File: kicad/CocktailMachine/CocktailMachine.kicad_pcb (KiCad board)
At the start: 2 copper layers, 66 parts, among them J1 Conn_01x08_Male, J2 0022232041, J3 3220-10-0100-00, J4 Barrel_Jack_Switch, J5 105-1102-001, J6 105-1103-001, J7 0022232041, U1 ESP32-WROOM-32, U2 TXB0104PWR, U3 MCP6477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

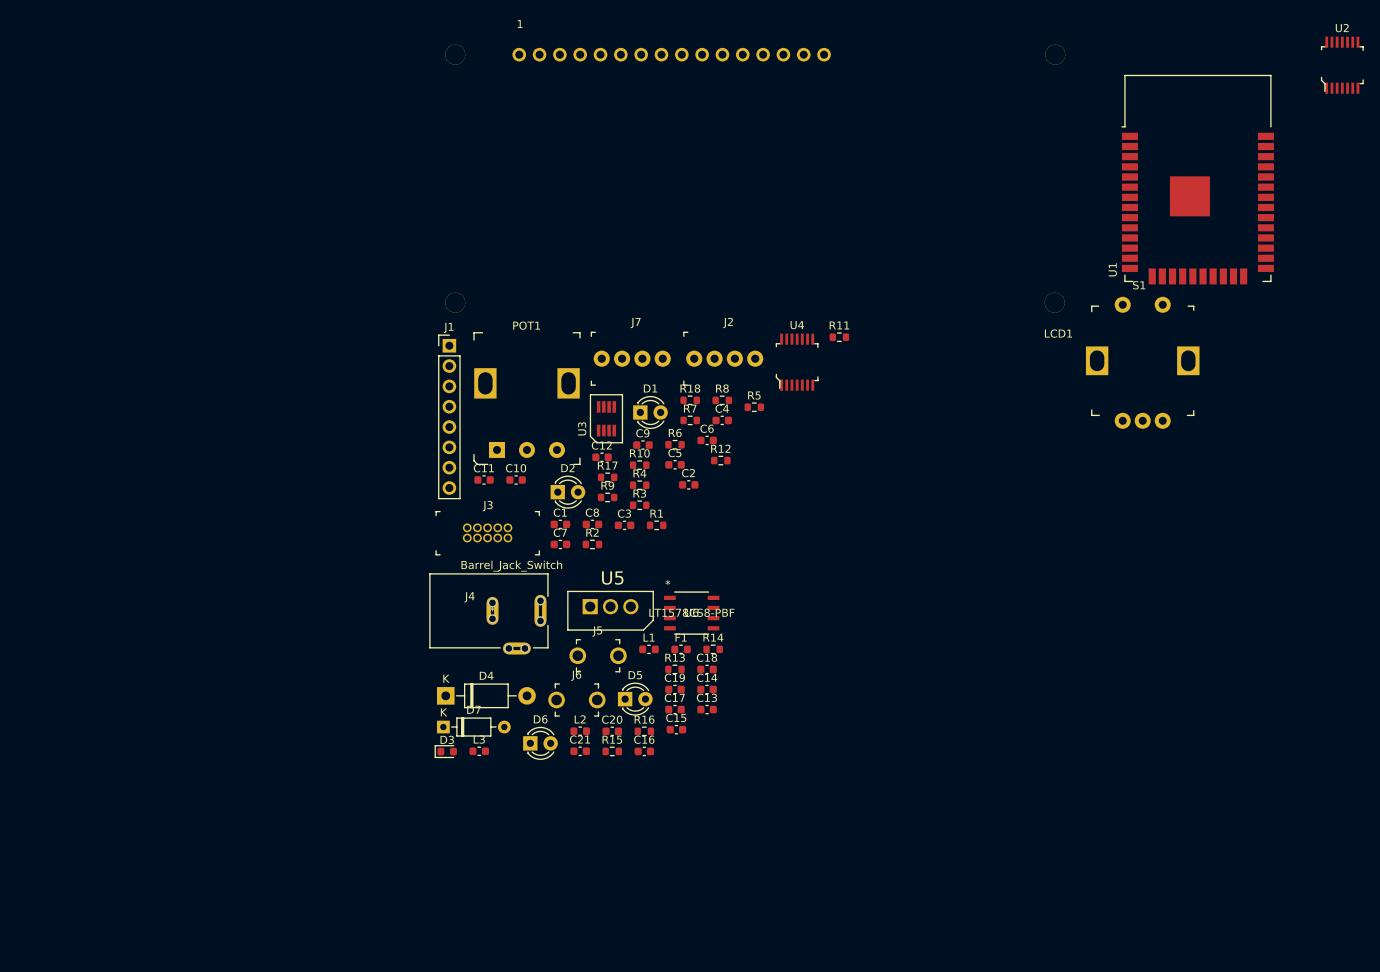
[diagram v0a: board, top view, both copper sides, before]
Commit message: - Update symbol and footprint library - Update obsolete components - Initial layout positioning done. Todo: routing
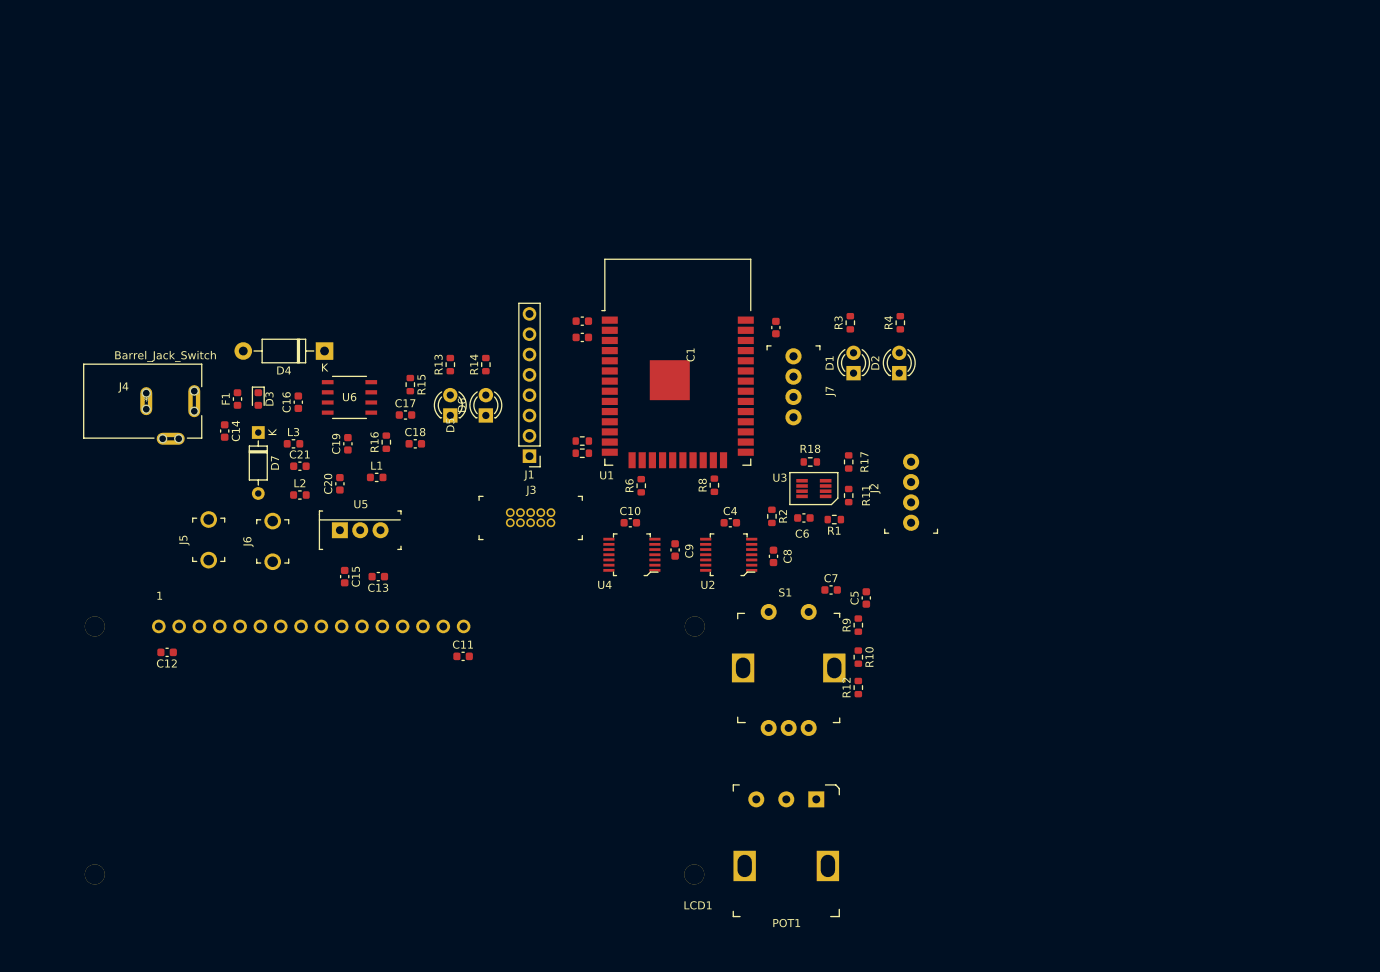
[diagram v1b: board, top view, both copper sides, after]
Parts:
- U5: value MCP1826S-3302e/AB -> LD1117V33; footprint MCP1826S-3302E_AB:TO254P482X1024X3124-3P -> digikey-footprints:TO-220-3
- moved U2 98.1 mm to (135.8, 89.2), turned to 90 degrees
- moved LCD1 84.5 mm to (95.6, 114.2)
- moved U1 69.0 mm to (129.4, 68.1)
- moved C14 68.4 mm to (72.8, 73.7), turned to -90 degrees
- moved F1 63.7 mm to (74.4, 69.7), turned to 90 degrees
- moved C16 61.5 mm to (82.0, 70.1), turned to 90 degrees
- moved C12 59.6 mm to (65.6, 101.4), turned to 180 degrees
- moved POT1 59.2 mm to (146.8, 119.8), turned to 180 degrees
- moved S1 58.6 mm to (137.6, 103.3)
- moved R15 52.3 mm to (96.0, 67.9), turned to -90 degrees
- moved C19 51.1 mm to (88.2, 75.3), turned to 90 degrees
- moved J5 50.8 mm to (70.8, 87.3), turned to 90 degrees
- moved J4 50.6 mm to (63.0, 70.0)
- moved U6 50.6 mm to (88.4, 69.5)
- moved D3 50.0 mm to (77.0, 69.7), turned to -90 degrees
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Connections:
- J3 pad 10: Net-(J3-Pad10) -> unconnected-(J3-Pad10)
- J3 pad 7: Net-(J3-Pad7) -> unconnected-(J3-Pad7)
- LCD1 pad 10: Net-(LCD1-Pad10) -> unconnected-(LCD1-Pad10)
- LCD1 pad 7: Net-(LCD1-Pad7) -> unconnected-(LCD1-Pad7)
- LCD1 pad 8: Net-(LCD1-Pad8) -> unconnected-(LCD1-Pad8)
- LCD1 pad 9: Net-(LCD1-Pad9) -> unconnected-(LCD1-Pad9)
- POT1 pad 2: Net-(POT1-Pad2) -> unconnected-(POT1-Pad2)
- POT1 pad 4: Net-(POT1-Pad4) -> unconnected-(POT1-Pad4)
- U1 pad 29: Net-(U1-Pad29) -> unconnected-(U1-Pad29)
- U1 pad 32: Net-(U1-Pad32) -> unconnected-(U1-Pad32)
- U1 pad 36: Net-(U1-Pad36) -> unconnected-(U1-Pad36)
- U2 pad 10: Net-(U2-Pad10) -> unconnected-(U2-Pad10)
- U2 pad 5: Net-(U2-Pad5) -> unconnected-(U2-Pad5)
- U2 pad 6: Net-(U2-Pad6) -> unconnected-(U2-Pad6)
- U2 pad 9: Net-(U2-Pad9) -> unconnected-(U2-Pad9)
- U4 pad 6: Net-(U4-Pad6) -> unconnected-(U4-Pad6)
- U4 pad 9: Net-(U4-Pad9) -> unconnected-(U4-Pad9)
- U5 pad 1: +5V -> GND
- U5 pad 2: GND -> +3V3
- U5 pad 3: +3V3 -> +5V
- U6 pad 7: Net-(U6-Pad7) -> unconnected-(U6-Pad7)
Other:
- net class Default removed

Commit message: - Fix DRC violations - Shrink space between modules to reduce board size
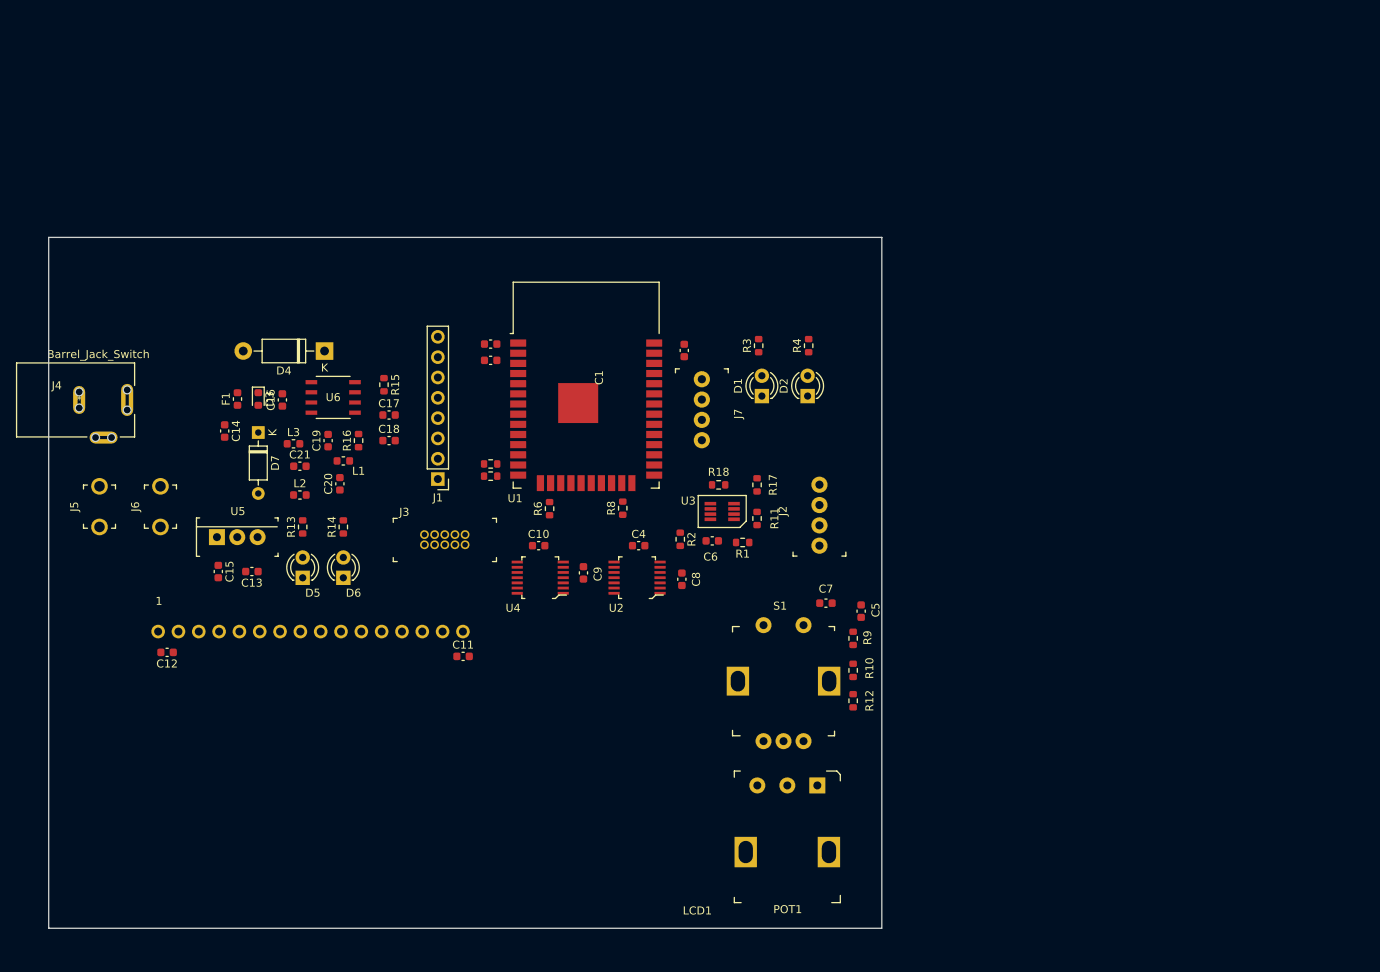
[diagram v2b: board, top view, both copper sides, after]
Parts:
- moved D5 27.4 mm to (82.5, 92.1)
- moved R13 27.4 mm to (82.5, 85.7)
- moved D6 27.0 mm to (87.6, 92.1)
- moved R14 27.0 mm to (87.6, 85.7)
- moved C13 15.8 mm to (76.2, 91.3)
- moved C15 15.8 mm to (72.0, 91.3)
- moved U5 15.4 mm to (71.8, 87.0)
- moved J6 14.7 mm to (64.8, 83.2)
- moved J5 14.3 mm to (57.1, 83.2)
- moved J7 11.8 mm to (132.4, 67.3)
- moved R1 11.8 mm to (137.5, 87.7)
- moved R11 11.8 mm to (139.3, 84.7)
- moved R17 11.8 mm to (139.3, 80.5)
- moved R18 11.8 mm to (134.5, 80.5)
- moved C8 11.8 mm to (129.9, 92.3)
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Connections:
- POT1 pad 2: unconnected-(POT1-Pad2) -> /V0_DISPLAY_CONTRAST
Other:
- board outline added: 104.1 x 86.4 mm

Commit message: - Finish layout - Fixed all DRC violations minus silkscreen issues - Updated via sizes to meet PCBWay requirements
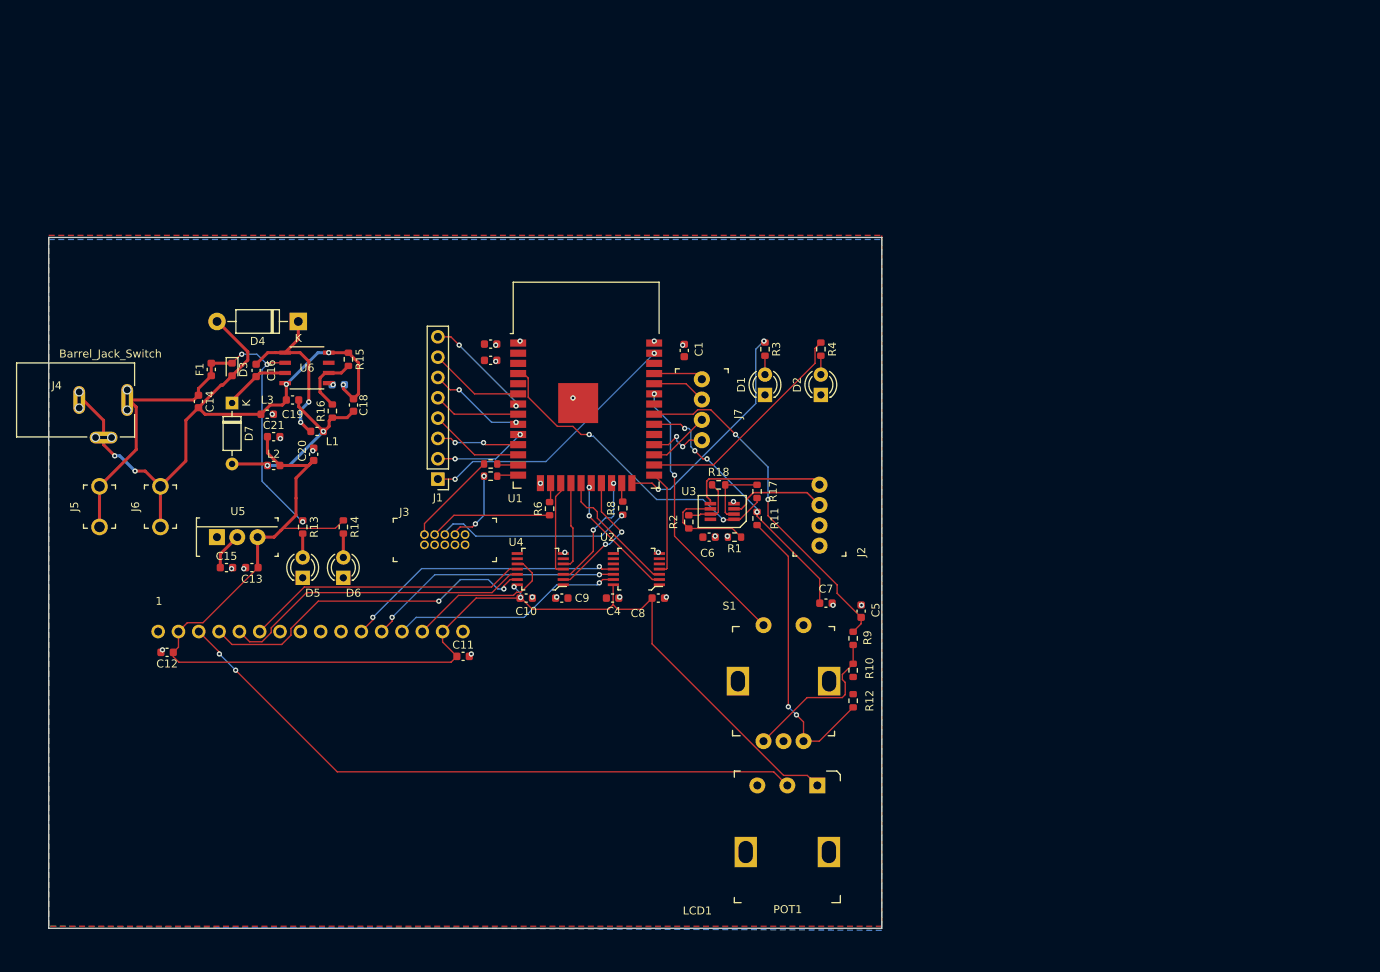
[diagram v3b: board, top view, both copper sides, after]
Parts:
- C17: moved to B.Cu
- moved C17 7.39 mm to (87.0, 67.9)
- moved C4 7.32 mm to (121.3, 94.6)
- moved C19 6.75 mm to (81.3, 69.8), turned to 180 degrees
- moved C10 6.73 mm to (110.5, 94.6)
- moved C18 6.29 mm to (88.9, 70.5), turned to 90 degrees
- moved R15 5.46 mm to (88.3, 64.8)
- moved C21 4.94 mm to (78.9, 74.4)
- moved R16 4.94 mm to (86.3, 71.2)
- moved D4 4.94 mm to (82.0, 60.0)
- moved C14 4.94 mm to (69.5, 70.0)
- moved C16 4.94 mm to (76.7, 66.2)
- moved C20 4.94 mm to (83.9, 76.6)
- moved D3 4.94 mm to (73.7, 66.0)
- moved D7 4.94 mm to (73.7, 70.2)
- moved F1 4.94 mm to (71.1, 66.0)
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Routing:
- net +5V: track 0.00 -> 158.6 mm, vias 0 -> 2
- net /V0_DISPLAY_CONTRAST: track 0.00 -> 81.7 mm, vias 0 -> 2
- net GND1: track 0.00 -> 80.9 mm, vias 0 -> 5
- net +12V: track 0.00 -> 64.6 mm, vias 0 -> 3
- net /ENCODER_A: track 0.00 -> 43.3 mm, vias 0 -> 2
- net /LCD_RS: track 0.00 -> 43.0 mm, vias 0 -> 2
- net /LOAD_CELL_ADC1_CH0: track 0.00 -> 40.3 mm, vias 0 -> 2
- net /LCD_RW: track 0.00 -> 39.1 mm
- net Net-(R11-Pad1): track 0.00 -> 37.4 mm, vias 0 -> 2
- net /LCD_EN: track 0.00 -> 35.4 mm
- net /LCD_DB4: track 0.00 -> 35.2 mm, vias 0 -> 2
- net /PUSHBUTTON_INPUT: track 0.00 -> 34.6 mm, vias 0 -> 2
- net /CTRL1: track 0.00 -> 33.6 mm, vias 0 -> 2
- net /ENCODER_B: track 0.00 -> 33.5 mm, vias 0 -> 4
- net /LCD_DB5: track 0.00 -> 32.2 mm, vias 0 -> 2
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- added copper zone on F.Cu, net +3V3
- added copper zone on B.Cu, net GND

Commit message: - Polygon pour zones for 3V3, 12V, and 5V - Add mounting holes - Finish routing and change to all 15 mil track widths
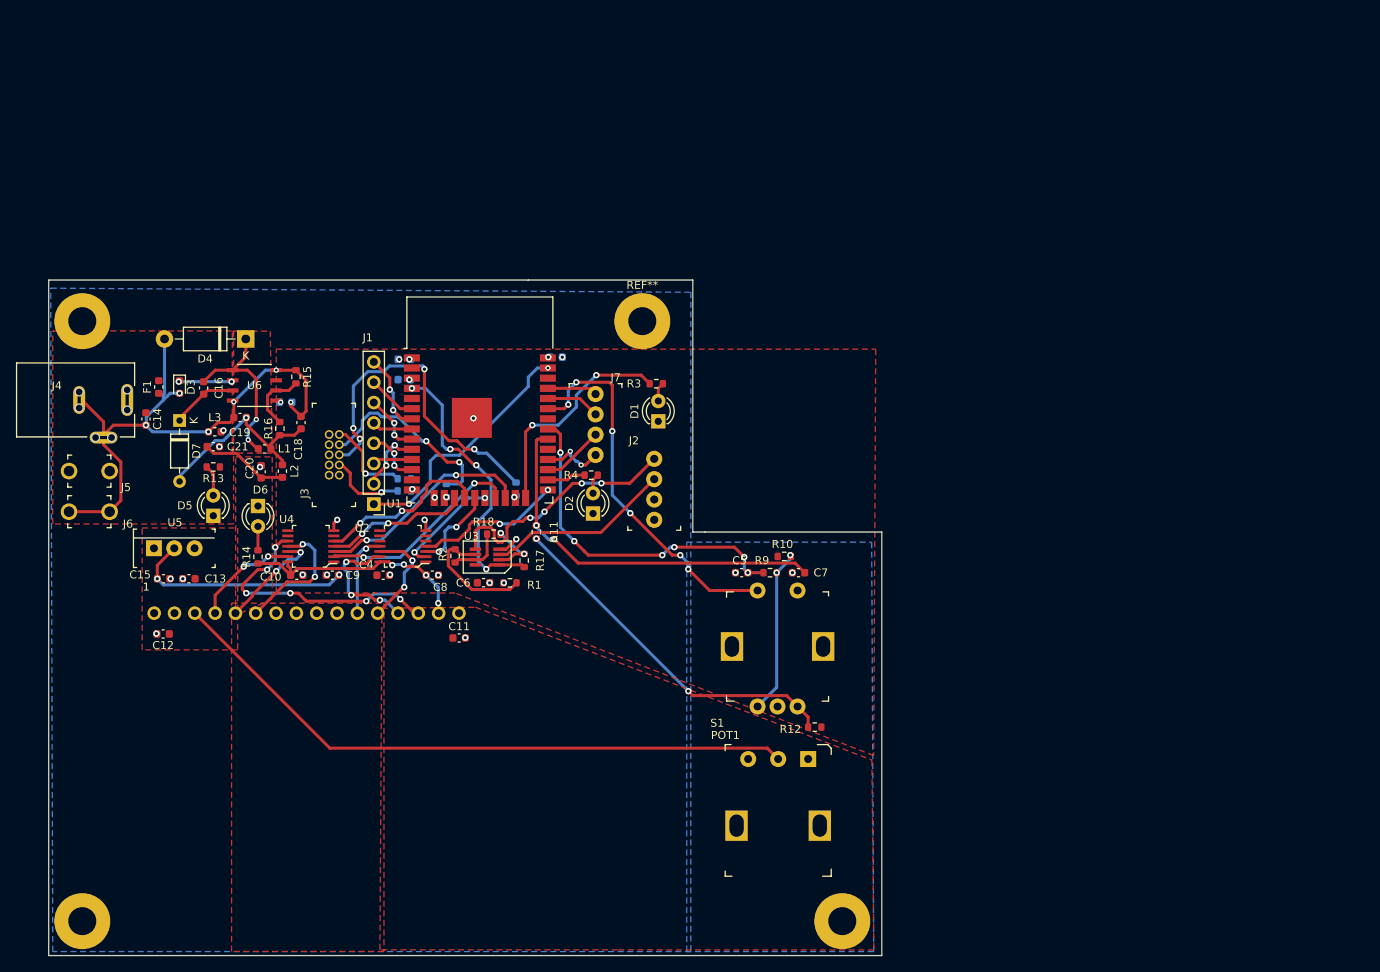
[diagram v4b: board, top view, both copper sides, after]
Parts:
- added ?: , , F.Cu at (55.0, 135.0)
- added ?: , , F.Cu at (150.0, 135.0)
- added ?: , , F.Cu at (55.0, 60.0)
- added REF**: MountingHole_3.5mm_Pad, MountingHole:MountingHole_3.5mm_Pad, F.Cu at (125.0, 60.0)
- C1, C2, C3, R5, R6, R7, R8: moved to B.Cu
- moved R4 32.7 mm to (118.6, 79.2), turned to 0 degrees
- moved D2 32.1 mm to (118.8, 84.0)
- moved R17 30.4 mm to (110.2, 89.9)
- moved U3 29.9 mm to (105.6, 89.5)
- moved R2 29.5 mm to (101.6, 89.3), turned to 90 degrees
- moved U2 29.3 mm to (95.1, 88.1)
- moved C4 28.8 mm to (92.6, 91.8)
- moved C9 28.8 mm to (86.3, 91.8)
- moved U4 28.8 mm to (83.6, 88.1)
- moved C10 28.8 mm to (81.8, 91.8)
- moved R18 28.8 mm to (106.4, 86.6)
- moved C6 28.8 mm to (105.2, 92.7)
- moved R1 28.6 mm to (108.5, 92.7)
- moved C8 28.4 mm to (98.8, 91.8)
- moved R11 27.6 mm to (111.8, 86.4)
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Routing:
- net +5V: track 158.6 -> 41.3 mm, vias 2 -> 4
- net +12V: track 64.6 -> 6.60 mm, vias 3 -> 2
- net /LCD_RS: track 43.0 -> 13.3 mm
- net /LCD_RW: track 39.1 -> 13.2 mm, vias 0 -> 2
- net /LCD_DB4: track 35.2 -> 10.5 mm, vias 2 -> 1
- net +3V3: track 4.69 -> 28.3 mm, vias 0 -> 5
- net /TEST_LED_1: track 28.3 -> 4.84 mm
- net /LCD_DB5: track 32.2 -> 13.0 mm
- net /LCD_EN: track 35.4 -> 16.4 mm, vias 0 -> 2
- net /TDO: track 24.5 -> 41.7 mm, vias 1 -> 4
- net /ENCODER_B: track 33.5 -> 48.2 mm, vias 4 -> 2
- net /LCD_DB7: track 19.7 -> 33.5 mm, vias 0 -> 6
- net /SENSE-: track 17.5 -> 31.3 mm, vias 0 -> 4
- net /PUSHBUTTON_INPUT: track 34.6 -> 47.9 mm, vias 2 -> 6
- net /LCD_DB6: track 29.1 -> 16.1 mm, vias 1 -> 3
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- added copper zone on F.Cu, net +12V
- added copper zone on F.Cu, net +5V
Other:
- board size 104.1 x 86.4 mm -> 104.1 x 84.4 mm
